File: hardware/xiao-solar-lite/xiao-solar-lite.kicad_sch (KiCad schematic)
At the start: 36 parts, among them J1 SOLAR, J3 OUT (to Xiao 5V), J4 BATTERY, J5 I2C + CE, Q2 AO3400A (ship FET), U1 BQ25798RQMR

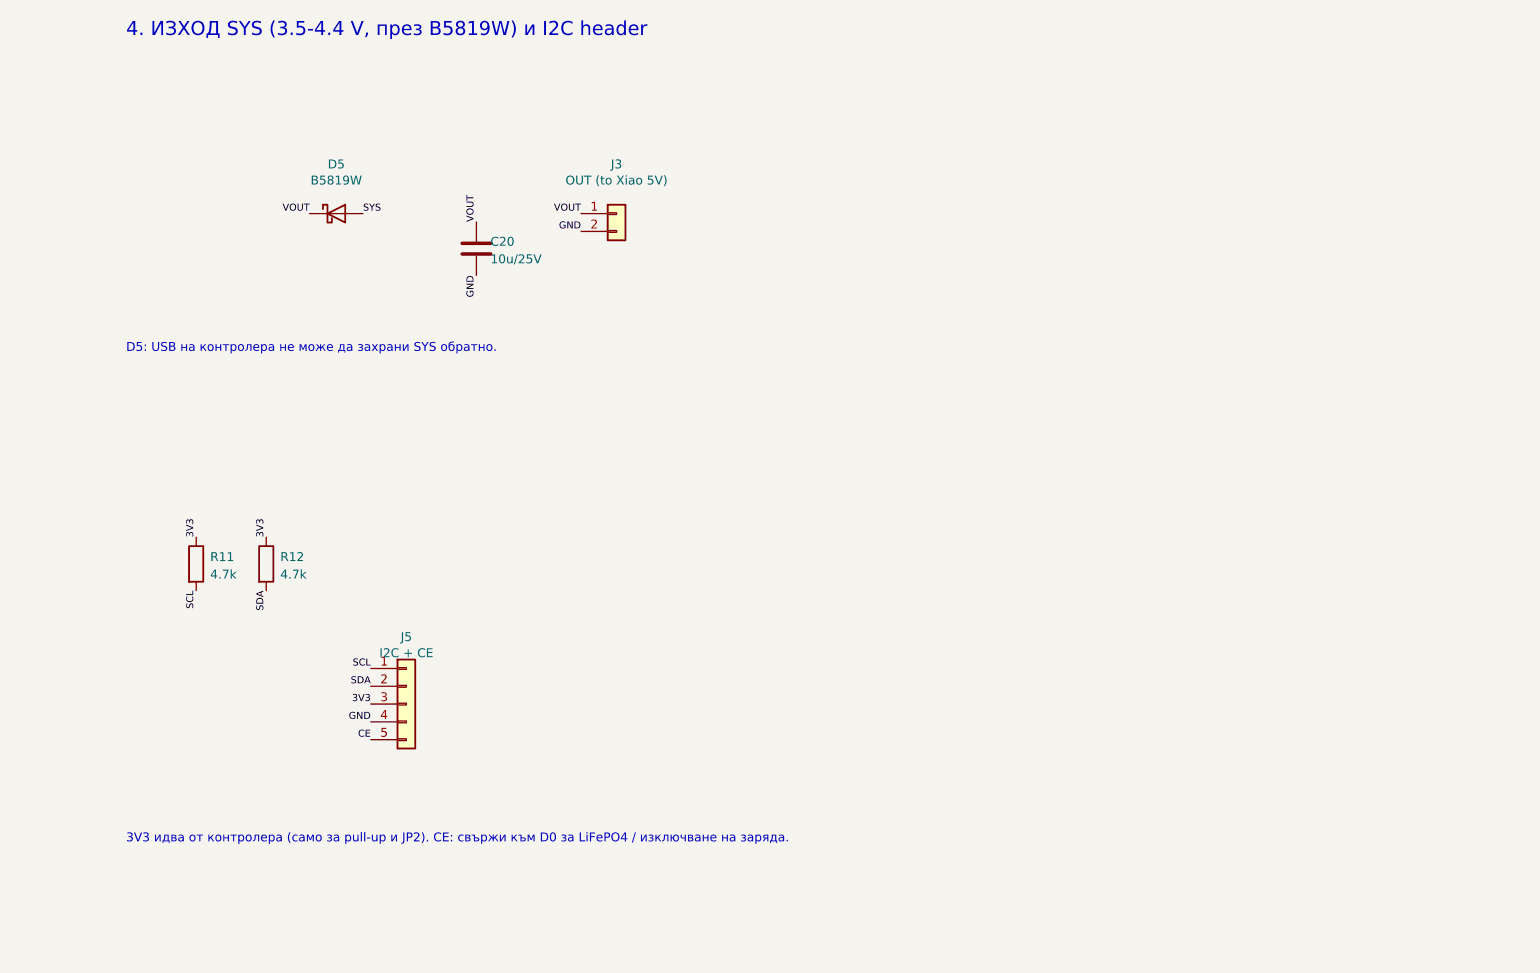
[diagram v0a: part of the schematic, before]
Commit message: hardware: xiao-solar-lite v0.2 as third layer under XIAO + Wio
The module now stacks under the standard XIAO nRF52840 + Wio-SX1262
sandwich through the 14 XIAO holes: CE on D0, SCL/SDA on D6/D7, 3V3,
GND, and SYS through B5819W to the 5V pin. 23 x 53 mm, charger below the
stack, only flat parts under it. Separate 4-pin I2C header for sensors.
Keepouts keep signal tracks off the L1 switch node and off the edge.

Co-Authored-By: Claude Opus 5.5 <noreply@anthropic.com>
Claude-Session: https://claude.ai/code/session_01P5Km81NY9NPL6RpKFGVEbH
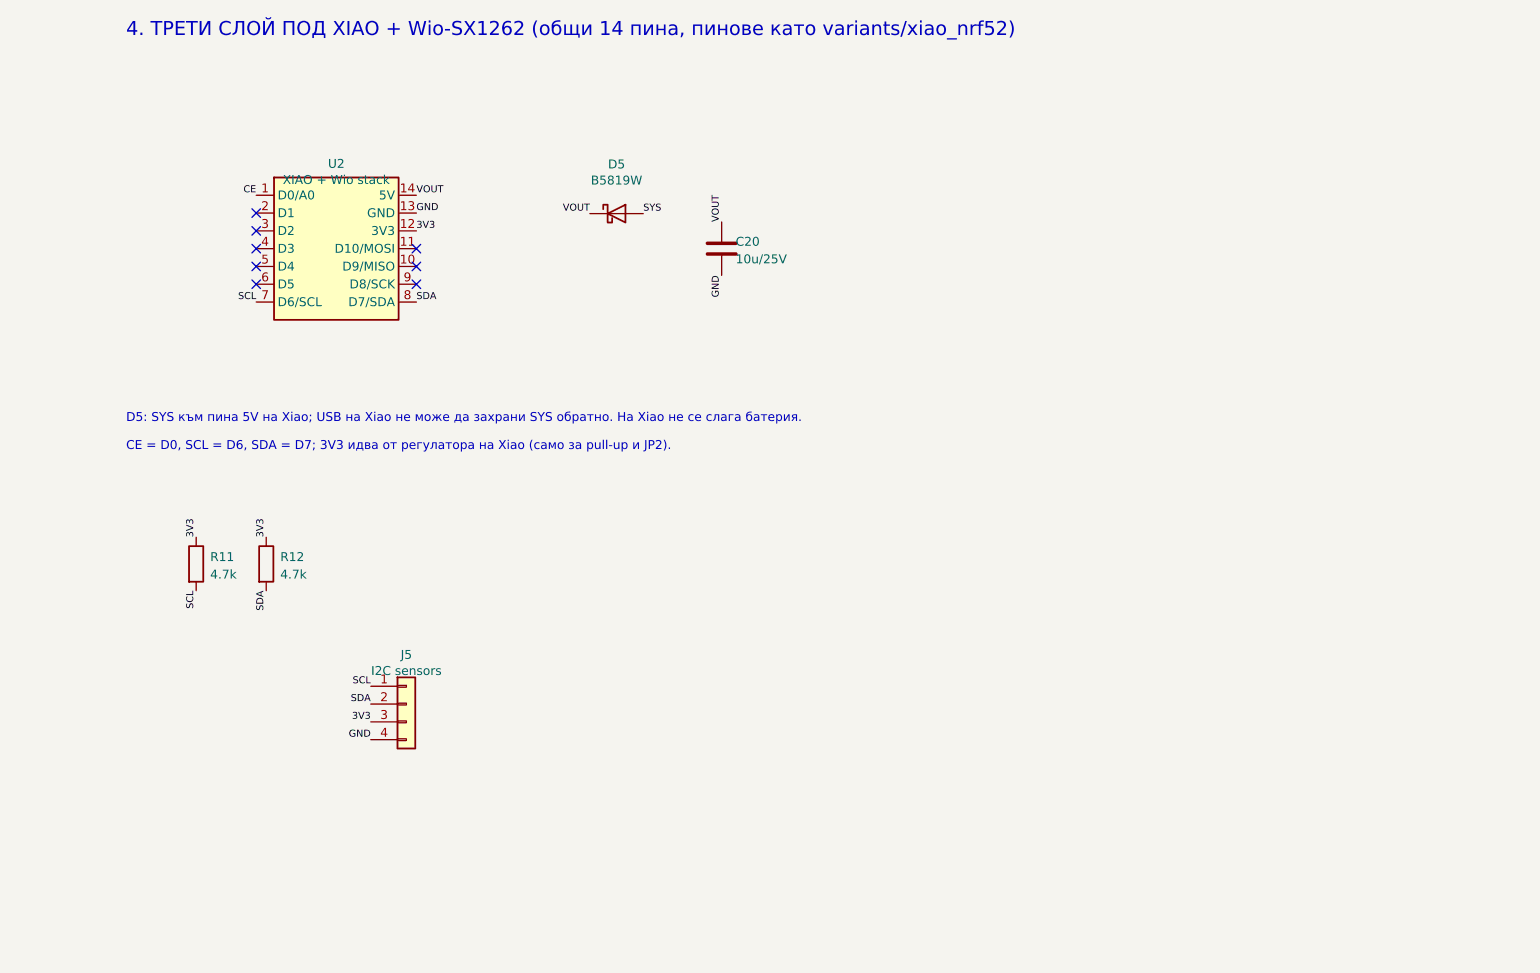
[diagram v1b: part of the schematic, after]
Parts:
- removed J3: OUT (to Xiao 5V), Connector_PinHeader_2.54mm:PinHeader_1x02_P2.54mm_Vertical, symbol Connector_Generic:Conn_01x02
- removed J5: I2C + CE, Connector_PinHeader_2.54mm:PinHeader_1x05_P2.54mm_Vertical, symbol Connector_Generic:Conn_01x05
- added J5: I2C sensors, Connector_PinHeader_2.54mm:PinHeader_1x04_P2.54mm_Vertical, symbol Connector_Generic:Conn_01x04
- added U2: XIAO + Wio stack, xiao_solar:XIAO_14P_2.54_21x17.8mm, symbol xiao_solar:XIAO_nRF52840
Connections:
- net 3V3: now also J5.3 (Pin_3), U2.12 (3V3)
- net CE: now also U2.1 (D0/A0)
- net GND: now also J5.4 (Pin_4), U2.13 (GND)
- net SCL: now also J5.1 (Pin_1), U2.7 (D6/SCL)
- net SDA: now also J5.2 (Pin_2), U2.8 (D7/SDA)
- net VOUT: now also U2.14 (5V)
- no-connect marks 3 -> 11
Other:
- note added: "4. ТРЕТИ СЛОЙ ПОД XIAO + Wio-SX1262 (общи 14 пина, пинове като variants/xiao_nrf52)"
- note added: "CE = D0, SCL = D6, SDA = D7; 3V3 идва от регулатора на Xiao (само за pull-up и JP2)."
- note added: "D5: SYS към пина 5V на Xiao; USB на Xiao не може да захрани SYS обратно. На Xiao не се слага батерия."
- note removed: "3V3 идва от контролера (само за pull-up и JP2). CE: свържи към D0 за LiFePO4 / изключване на заряда."
- note removed: "4. ИЗХОД SYS (3.5-4.4 V, през B5819W) и I2C header"
- note removed: "D5: USB на контролера не може да захрани SYS обратно."
- title: Solar charger module lite (BQ25798, I2C) -> Solar charger layer for XIAO + Wio (BQ25798)

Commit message: hardware: charger zone per BQ25798 layout guide, v0.3 of both boards
- tools/charger.py: shared BQ25798 cluster (placement, PMID/SYS/VBUS/BAT/SW
  copper zones, hand routes) for xiao-solar and xiao-solar-lite
- 100 nF PMID/SYS caps at the pins, SW short and wide to L1, BTST/REGN/GND
  through vias under the package, BAT halves joined on B.Cu
- lite: TI cap counts (VBUS 2, PMID 3, SYS 5), 23 x 57 mm, D5 fed from SYS
- thermal spokes on small parts, solid on charger power caps
- routing: zone copper goes to Freerouting as fixed hatched wires, locked
  hand routes survive the finish pass; JLC CPL rotation fix for SOT-23/LED
- both boards 0 unconnected; READMEs, Gerber, BOM, CPL, PDFs, images

Co-Authored-By: Claude Opus 5.5 <noreply@anthropic.com>
Claude-Session: https://claude.ai/code/session_01P5Km81NY9NPL6RpKFGVEbH
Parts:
- added C14, C15: 10u/25V, Capacitor_SMD:C_0805_2012Metric, symbol Device:C
- added C2, C8: 10u/50V, Capacitor_SMD:C_1206_3216Metric, symbol Device:C
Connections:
- net GND: now also C14.2, C15.2, C2.2, C8.2
- net PMID: now also C8.1
- net SYS: now also C14.1, C15.1
- net VBUS: now also C2.1
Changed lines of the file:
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@@
 (kicad_sch (version 20230121) (generator eeschema)
   (paper "A3")
-  (title_block (title "Solar charger layer for XIAO + Wio (BQ25798)") (date "2026-10-29") (rev "0.1") (company "n3tk0/MeshCore"))
+  (title_block (title "Solar charger layer for XIAO + Wio (BQ25798)") (date "2026-10-29") (rev "0.3") (company "n3tk0/MeshCore"))
   (symbol (lib_id "Connector_Generic:Conn_01x02") (at 20 35 0) (unit 1) (in_bom yes) (on_board yes) (dnp no)
     (property "Reference" "J1" (at 20 27.96 0) (effects (font (size 1.27 1.27))))
@@
     (pin "2")
     (instances (project "xiao-solar-lite" (path "/6b1f3c1e-6a5e-4b7e-9d65-5f0b3a1d0002" (reference "C1") (unit 1))))
+  )
+  (symbol (lib_id "Device:C") (at 88 40 0) (unit 1) (in_bom yes) (on_board yes) (dnp no)
+    (property "Reference" "C2" (at 90 39 0) (effects (font (size 1.27 1.27)) (justify left)))
+    (property "Value" "10u/50V" (at 90 41.5 0) (effects (font (size 1.27 1.27)) (justify left)))
+    (property "Footprint" "Capacitor_SMD:C_1206_3216Metric" (at 88 40 0) (effects (font (size 1.27 1.27)) hide))
+    (property "Datasheet" "" (at 88 40 0) (effects (font (size 1.27 1.27)) hide))
+    (property "LCSC" "C13585" (at 88 40 0) (effects (font (size 1.27 1.27)) hide))
+    (pin "1")
+    (pin "2")
+    (instances (project "xiao-solar-lite" (path "/6b1f3c1e-6a5e-4b7e-9d65-5f0b3a1d0002" (reference "C2") (unit 1))))
   )
   (symbol (lib_id "Device:C") (at 98 40 0) (unit 1) (in_bom yes) (on_board yes) (dnp no)
@@
     (instances (project "xiao-solar-lite" (path "/6b1f3c1e-6a5e-4b7e-9d65-5f0b3a1d0002" (reference "C7") (unit 1))))
   )
+  (symbol (lib_id "Device:C") (at 126 140 0) (unit 1) (in_bom yes) (on_board yes) (dnp no)
+    (property "Reference" "C8" (at 128 139 0) (effects (font (size 1.27 1.27)) (justify left)))
+    (property "Value" "10u/50V" (at 128 141.5 0) (effects (font (size 1.27 1.27)) (justify left)))
+    (property "Footprint" "Capacitor_SMD:C_1206_3216Metric" (at 126 140 0) (effects (font (size 1.27 1.27)) hide))
+    (property "Datasheet" "" (at 126 140 0) (effects (font (size 1.27 1.27)) hide))
+    (property "LCSC" "C13585" (at 126 140 0) (effects (font (size 1.27 1.27)) hide))
+    (pin "1")
+    (pin "2")
+    (instances (project "xiao-solar-lite" (path "/6b1f3c1e-6a5e-4b7e-9d65-5f0b3a1d0002" (reference "C8") (unit 1))))
+  )
   (symbol (lib_id "Device:C") (at 134 140 0) (unit 1) (in_bom yes) (on_board yes) (dnp no)
     (property "Reference" "C9" (at 136 139 0) (effects (font (size 1.27 1.27)) (justify left)))
@@
     (pin "2")
     (instances (project "xiao-solar-lite" (path "/6b1f3c1e-6a5e-4b7e-9d65-5f0b3a1d0002" (reference "C13") (unit 1))))
+  )
+  (symbol (lib_id "Device:C") (at 134 160 0) (unit 1) (in_bom yes) (on_board yes) (dnp no)
+    (property "Reference" "C14" (at 136 159 0) (effects (font (size 1.27 1.27)) (justify left)))
+    (property "Value" "10u/25V" (at 136 161.5 0) (effects (font (size 1.27 1.27)) (justify left)))
+    (property "Footprint" "Capacitor_SMD:C_0805_2012Metric" (at 134 160 0) (effects (font (size 1.27 1.27)) hide))
+    (property "Datasheet" "" (at 134 160 0) (effects (font (size 1.27 1.27)) hide))
+    (property "LCSC" "C15850" (at 134 160 0) (effects (font (size 1.27 1.27)) hide))
+    (pin "1")
+    (pin "2")
+    (instances (project "xiao-solar-lite" (path "/6b1f3c1e-6a5e-4b7e-9d65-5f0b3a1d0002" (reference "C14") (unit 1))))
+  )
+  (symbol (lib_id "Device:C") (at 142 160 0) (unit 1) (in_bom yes) (on_board yes) (dnp no)
+    (property "Reference" "C15" (at 144 159 0) (effects (font (size 1.27 1.27)) (justify left)))
+    (property "Value" "10u/25V" (at 144 161.5 0) (effects (font (size 1.27 1.27)) (justify left)))
+    (property "Footprint" "Capacitor_SMD:C_0805_2012Metric" (at 142 160 0) (effects (font (size 1.27 1.27)) hide))
+    (property "Datasheet" "" (at 142 160 0) (effects (font (size 1.27 1.27)) hide))
+    (property "LCSC" "C15850" (at 142 160 0) (effects (font (size 1.27 1.27)) hide))
+    (pin "1")
+    (pin "2")
+    (instances (project "xiao-solar-lite" (path "/6b1f3c1e-6a5e-4b7e-9d65-5f0b3a1d0002" (reference "C15") (unit 1))))
   )
   (symbol (lib_id "Device:C") (at 150 160 0) (unit 1) (in_bom yes) (on_board yes) (dnp no)
@@
   (label "VBUS" (at 78 36.19 90) (fields_autoplaced) (effects (font (size 1.0 1.0)) (justify left bottom)))
   (label "GND" (at 78 43.81 270) (fields_autoplaced) (effects (font (size 1.0 1.0)) (justify right bottom)))
+  (label "VBUS" (at 88 36.19 90) (fields_autoplaced) (effects (font (size 1.0 1.0)) (justify left bottom)))
+  (label "GND" (at 88 43.81 270) (fields_autoplaced) (effects (font (size 1.0 1.0)) (justify right bottom)))
   (label "VBUS" (at 98 36.19 90) (fields_autoplaced) (effects (font (size 1.0 1.0)) (justify left bottom)))
   (label "GND" (at 98 43.81 270) (fields_autoplaced) (effects (font (size 1.0 1.0)) (justify right bottom)))
@@
   (label "PMID" (at 118 136.19 90) (fields_autoplaced) (effects (font (size 1.0 1.0)) (justify left bottom)))
   (label "GND" (at 118 143.81 270) (fields_autoplaced) (effects (font (size 1.0 1.0)) (justify right bottom)))
+  (label "PMID" (at 126 136.19 90) (fields_autoplaced) (effects (font (size 1.0 1.0)) (justify left bottom)))
+  (label "GND" (at 126 143.81 270) (fields_autoplaced) (effects (font (size 1.0 1.0)) (justify right bottom)))
   (label "PMID" (at 134 136.19 90) (fields_autoplaced) (effects (font (size 1.0 1.0)) (justify left bottom)))
   (label "GND" (at 134 143.81 270) (fields_autoplaced) (effects (font (size 1.0 1.0)) (justify right bottom)))
@@
   (label "SYS" (at 126 156.19 90) (fields_autoplaced) (effects (font (size 1.0 1.0)) (justify left bottom)))
   (label "GND" (at 126 163.81 270) (fields_autoplaced) (effects (font (size 1.0 1.0)) (justify right bottom)))
+  (label "SYS" (at 134 156.19 90) (fields_autoplaced) (effects (font (size 1.0 1.0)) (justify left bottom)))
+  (label "GND" (at 134 163.81 270) (fields_autoplaced) (effects (font (size 1.0 1.0)) (justify right bottom)))
+  (label "SYS" (at 142 156.19 90) (fields_autoplaced) (effects (font (size 1.0 1.0)) (justify left bottom)))
+  (label "GND" (at 142 163.81 270) (fields_autoplaced) (effects (font (size 1.0 1.0)) (justify right bottom)))
   (label "SYS" (at 150 156.19 90) (fields_autoplaced) (effects (font (size 1.0 1.0)) (justify left bottom)))
   (label "GND" (at 150 163.81 270) (fields_autoplaced) (effects (font (size 1.0 1.0)) (justify right bottom)))

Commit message: hardware: xiao-solar v0.4 (no loads, INA219, 48x71.5) + block schematics for both boards
Co-Authored-By: Claude Opus 5.5 <noreply@anthropic.com>
Claude-Session: https://claude.ai/code/session_01P5Km81NY9NPL6RpKFGVEbH
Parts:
- removed D5: B5819W, Diode_SMD:D_SOD-123, symbol Device:D_Schottky
- added D5: LM66100, Package_TO_SOT_SMD:SOT-363_SC-70-6, symbol xiao_solar:LM66100
- added JP3: no ship FET (LiFePO4), Jumper:SolderJumper-2_P1.3mm_Open_RoundedPad1.0x1.5mm, symbol Jumper:SolderJumper_2_Open
- added TP10: SDA, TestPoint:TestPoint_Pad_D1.0mm, symbol Connector:TestPoint
- added TP3: VBUS, TestPoint:TestPoint_Pad_D1.0mm, symbol Connector:TestPoint
- added TP4: PMID, TestPoint:TestPoint_Pad_D1.0mm, symbol Connector:TestPoint
- added TP5: SYS, TestPoint:TestPoint_Pad_D1.0mm, symbol Connector:TestPoint
- added TP6: BAT, TestPoint:TestPoint_Pad_D1.0mm, symbol Connector:TestPoint
- added TP7: GND, TestPoint:TestPoint_Pad_D1.0mm, symbol Connector:TestPoint
- added TP8: 3V3, TestPoint:TestPoint_Pad_D1.0mm, symbol Connector:TestPoint
- added TP9: SCL, TestPoint:TestPoint_Pad_D1.0mm, symbol Connector:TestPoint
- C16: footprint Capacitor_SMD:C_0603_1608Metric -> Capacitor_SMD:C_0402_1005Metric; LCSC C14663 -> C1525
- C9: value 100n -> 100n/50V; footprint Capacitor_SMD:C_0603_1608Metric -> Capacitor_SMD:C_0402_1005Metric; LCSC C14663 -> C131394
- D1: value SS34 -> SS54; LCSC C8678 -> C22452
- L1: value 2.2uH 3.2A -> 2.2uH 4A molded (MWSA0402S); footprint xiao_solar:IND-SMD_L4.0-W4.0_FNR40XXS -> xiao_solar:IND-SMD_L4.4-W4.2_MWSA0402S; LCSC C167869 -> C408335
- TP2: value QON (to GND = wake) -> QON
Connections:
- net 3V3: now also TP8.1
- net BAT: now also JP3.1 (A), TP6.1
- net BATT+: now also JP3.2 (B)
- net GND: now also D5.2 (GND), D5.4 (NC), D5.5 (~{ST}), TP7.1
- net PMID: now also TP4.1
- net SCL: now also TP9.1
- net SDA: now also TP10.1
- net SYS: now also D5.1 (VIN), TP5.1
- net VBUS: now also TP3.1
- net VOUT: now also D5.3 (~{CE}), D5.6 (VOUT)
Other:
- note added: "3V3 идва от регулатора на Xiao (само за pull-up и JP2)."
- note added: "5. I2C (CE=D0, SCL=D6, SDA=D7): BQ25798 0x6B, външни сензори"
- note added: "6. Тест точки за първото пускане (падове 1 mm отгоре)"
- note added: "INT не е изведен (firmware чете регистрите). Watchdog off. TP2 (QON) към GND за 1 s = събуждане от ship mode."
- note added: "PWR_FLAG"
- note added: "Q2: D към батерията, S към BAT; в shutdown (SDRV_CTRL=01, 0.5 uA)"
- note added: "SS54: защита от обратна полярност и от връщане към панела. VAC1=VAC2=VBUS, ACDRV към GND."
- note added: "Без NTC и без DW01A: клетката трябва да е със собствена защита."
- note added: "диодът на Q2 спира разреждането; събужда се, когато панелът даде напрежение."
- note removed: "CE = D0, SCL = D6, SDA = D7; 3V3 идва от регулатора на Xiao (само за pull-up и JP2)."
- note removed: "INT не е изведен (firmware чете регистрите). Watchdog off. Без NTC и без DW01A: клетката трябва да е със собствена защита."
- note removed: "SS34: защита от обратна полярност и от връщане към панела. VAC1=VAC2=VBUS, ACDRV към GND."
